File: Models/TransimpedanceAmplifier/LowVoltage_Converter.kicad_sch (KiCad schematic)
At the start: 6 parts, among them U7 LM78L05, 5V, 5%, U9 LM79L05, -5V, 5%

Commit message: Save progress after a major refactoring
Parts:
- removed C5: 10 nF, symbol Device:C
- removed C6: 100 nF, symbol Device:C
- removed D4, D5: D_Schottky, symbol Device:D_Schottky
- removed U7: LM78L05, 5V, 5%, LP3_TEX, symbol LM78L:LM78L05ACZ_LFT1
- removed U9: LM79L05, -5V, 5%, LP3_TEX, symbol LM79L:LM79L05ACZ_LFT1
- added C10: 10 nF, symbol Device:C
- added C9: 1 uF, symbol Device:C
- added D10, D11: D_Schottky, symbol Device:D_Schottky
- added U10: LM78L05, 5V, 5%, LP3_TEX, symbol LM78L:LM78L05ACZ_LFT1
- added U8: TLV76133, 3.3V, 1%, DCY0004A-IPC_A, symbol TLV761:PTLV76118DCYR
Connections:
- net 5V: now also C10.1, D10.1 (K), D11.1 (K), U10.1 (OUTPUT), U8.3 (IN)
- net GND: now also C10.2, C9.2, D11.2 (A), U10.2 (GND), U8.1 (GND)
- new net 18V: U10.3 (INPUT)
- new net 3.3V: C9.1, D10.2 (A), U8.4 (OUT)
- no-connect marks 0 -> 1
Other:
- note added: "Dropout voltage: 0.9 V (typical), 1.6 V (max) Variation with load: 0.9 V (1.0 A) 0.7 V (0.8 A) 0.2 V (0.1 A) Dropout voltage exceeds expected value when Vout + 1.5 V < 4.0 V"

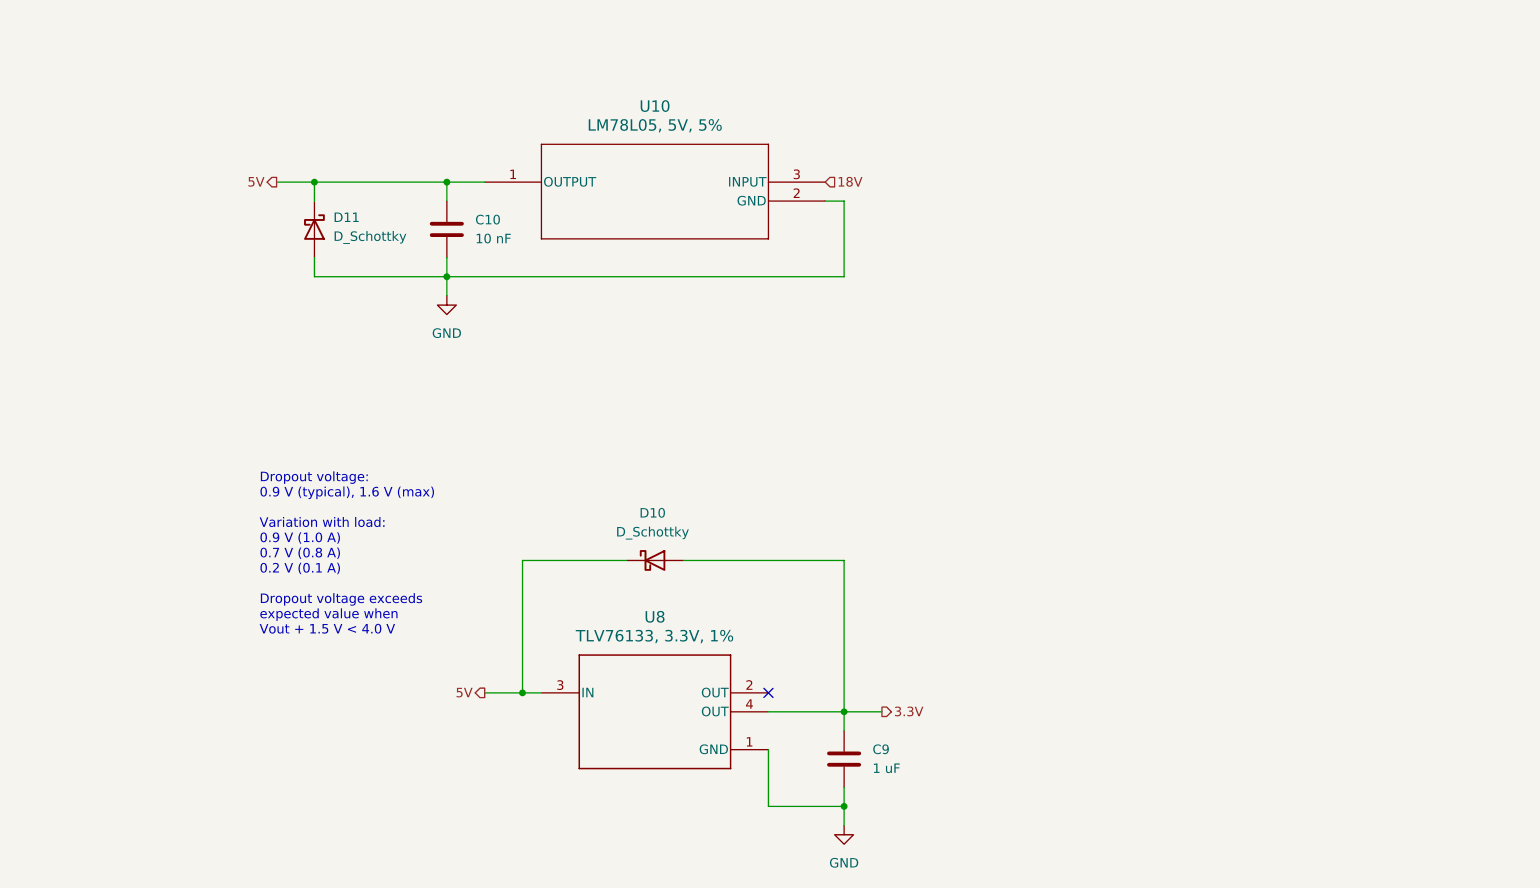
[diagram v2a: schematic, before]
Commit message: Added purchase links for all current capacitors, with dimensional tolerances matching the footprint
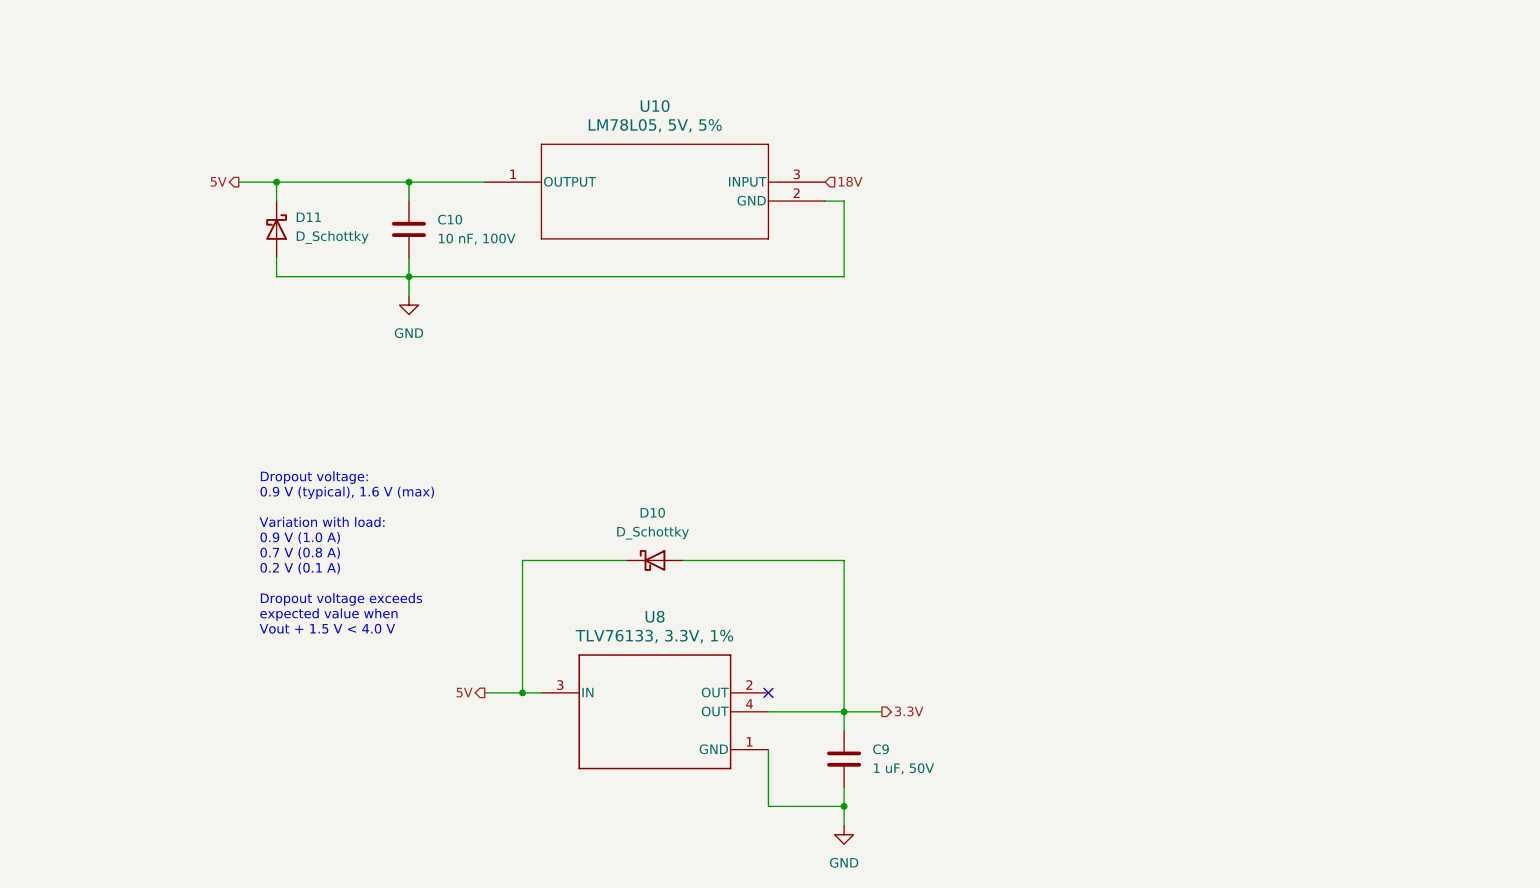
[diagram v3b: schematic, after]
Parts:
- C10: value 10 nF -> 10 nF, 100V; Purchase Link (none) -> https://www.digikey.com/en/products/detail/murata-electroni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
- C9: value 1 uF -> 1 uF, 50V; Purchase Link (none) -> https://www.digikey.com/en/products/detail/murata-electroni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
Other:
- moved on the sheet: C10, D11
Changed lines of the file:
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@@
 	)
 	(junction
-		(at 114.3 68.58)
+		(at 109.22 68.58)
 		(diameter 0)
 		(color 0 0 0 0)
 	)
 	(junction
-		(at 96.52 55.88)
+		(at 91.44 55.88)
 		(diameter 0)
 		(color 0 0 0 0)
 	)
 	(junction
-		(at 114.3 55.88)
+		(at 109.22 55.88)
 		(diameter 0)
 		(color 0 0 0 0)
@@
 	(wire
 		(pts
+			(xy 124.46 124.46) (xy 127 124.46)
+		)
+		(stroke
+			(width 0)
+			(type default)
+		)
+	)
+	(wire
+		(pts
+			(xy 167.64 127) (xy 167.64 129.54)
+		)
+		(stroke
+			(width 0)
+			(type default)
+		)
+	)
+	(wire
+		(pts
+			(xy 167.64 68.58) (xy 167.64 58.42)
+		)
+		(stroke
+			(width 0)
+			(type default)
+		)
+	)
+	(wire
+		(pts
+			(xy 119.38 124.46) (xy 124.46 124.46)
+		)
+		(stroke
+			(width 0)
+			(type default)
+		)
+	)
+	(wire
+		(pts
+			(xy 167.64 139.7) (xy 157.48 139.7)
+		)
+		(stroke
+			(width 0)
+			(type default)
+		)
+	)
+	(wire
+		(pts
+			(xy 138.43 106.68) (xy 124.46 106.68)
+		)
+		(stroke
+			(width 0)
+			(type default)
+		)
+	)
+	(wire
+		(pts
+			(xy 91.44 55.88) (xy 91.44 58.42)
+		)
+		(stroke
+			(width 0)
+			(type default)
+		)
+	)
+	(wire
+		(pts
+			(xy 157.48 127) (xy 167.64 127)
+		)
+		(stroke
+			(width 0)
+			(type default)
+		)
+	)
+	(wire
+		(pts
+			(xy 109.22 66.04) (xy 109.22 68.58)
+		)
+		(stroke
+			(width 0)
+			(type default)
+		)
+	)
+	(wire
+		(pts
+			(xy 109.22 55.88) (xy 119.38 55.88)
+		)
+		(stroke
+			(width 0)
+			(type default)
+		)
+	)
+	(wire
+		(pts
+			(xy 109.22 55.88) (xy 91.44 55.88)
+		)
+		(stroke
+			(width 0)
+			(type default)
+		)
+	)
+	(wire
+		(pts
+			(xy 167.64 137.16) (xy 167.64 139.7)
+		)
+		(stroke
+			(width 0)
+			(type default)
+		)
+	)
+	(wire
+		(pts
+			(xy 109.22 55.88) (xy 109.22 58.42)
+		)
+		(stroke
+			(width 0)
+			(type default)
+		)
+	)
+	(wire
+		(pts
 			(xy 165.1 58.42) (xy 167.64 58.42)
 		)
@@
 	(wire
 		(pts
-			(xy 124.46 124.46) (xy 127 124.46)
-		)
-		(stroke
-			(width 0)
-			(type default)
-		)
-	)
-	(wire
-		(pts
-			(xy 167.64 127) (xy 167.64 129.54)
-		)
-		(stroke
-			(width 0)
-			(type default)
-		)
-	)
-	(wire
-		(pts
-			(xy 119.38 124.46) (xy 124.46 124.46)
-		)
-		(stroke
-			(width 0)
-			(type default)
-		)
-	)
-	(wire
-		(pts
-			(xy 167.64 139.7) (xy 157.48 139.7)
-		)
-		(stroke
-			(width 0)
-			(type default)
-		)
-	)
-	(wire
-		(pts
-			(xy 138.43 106.68) (xy 124.46 106.68)
-		)
-		(stroke
-			(width 0)
-			(type default)
-		)
-	)
-	(wire
-		(pts
-			(xy 96.52 55.88) (xy 96.52 58.42)
-		)
-		(stroke
-			(width 0)
-			(type default)
-		)
-	)
-	(wire
-		(pts
-			(xy 114.3 68.58) (xy 167.64 68.58)
-		)
-		(stroke
-			(width 0)
-			(type default)
-		)
-	)
-	(wire
-		(pts
-			(xy 157.48 127) (xy 167.64 127)
-		)
-		(stroke
-			(width 0)
-			(type default)
-		)
-	)
-	(wire
-		(pts
-			(xy 114.3 66.04) (xy 114.3 68.58)
-		)
-		(stroke
-			(width 0)
-			(type default)
-		)
-	)
-	(wire
-		(pts
-			(xy 119.38 55.88) (xy 114.3 55.88)
-		)
-		(stroke
-			(width 0)
-			(type default)
-		)
-	)
-	(wire
-		(pts
-			(xy 114.3 55.88) (xy 96.52 55.88)
-		)
-		(stroke
-			(width 0)
-			(type default)
-		)
-	)
-	(wire
-		(pts
-			(xy 167.64 137.16) (xy 167.64 139.7)
-		)
-		(stroke
-			(width 0)
-			(type default)
-		)
-	)
-	(wire
-		(pts
-			(xy 114.3 55.88) (xy 114.3 58.42)
-		)
-		(stroke
-			(width 0)
-			(type default)
-		)
-	)
-	(wire
-		(pts
-			(xy 96.52 66.04) (xy 96.52 68.58)
+			(xy 109.22 68.58) (xy 167.64 68.58)
+		)
+		(stroke
+			(width 0)
+			(type default)
+		)
+	)
+	(wire
+		(pts
+			(xy 91.44 66.04) (xy 91.44 68.58)
 		)
 		(stroke
@@
 	(wire
 		(pts
-			(xy 91.44 55.88) (xy 96.52 55.88)
-		)
-		(stroke
-			(width 0)
-			(type default)
-		)
-	)
-	(wire
-		(pts
-			(xy 167.64 68.58) (xy 167.64 58.42)
+			(xy 86.36 55.88) (xy 91.44 55.88)
 		)
 		(stroke
@@
 	(wire
 		(pts
-			(xy 114.3 68.58) (xy 114.3 71.12)
-		)
-		(stroke
-			(width 0)
-			(type default)
-		)
-	)
-	(wire
-		(pts
-			(xy 96.52 68.58) (xy 114.3 68.58)
+			(xy 109.22 68.58) (xy 109.22 71.12)
+		)
+		(stroke
+			(width 0)
+			(type default)
+		)
+	)
+	(wire
+		(pts
+			(xy 91.44 68.58) (xy 109.22 68.58)
 		)
 		(stroke
@@
 	(hierarchical_label "5V"
 		(shape output)
-		(at 91.44 55.88 180)
+		(at 86.36 55.88 180)
 		(effects
 			(font
@@
 	(symbol
 		(lib_id "Device:C")
-		(at 114.3 62.23 0)
+		(at 109.22 62.23 0)
 		(unit 1)
 		(exclude_from_sim no)
@@
 		(fields_autoplaced yes)
 		(property "Reference" "C10"
-			(at 118.11 60.9599 0)
+			(at 113.03 60.9599 0)
 			(effects
 				(font
@@
 			)
 		)
-		(property "Value" "10 nF"
-			(at 118.11 63.4999 0)
+		(property "Value" "10 nF, 100V"
+			(at 113.03 63.4999 0)
 			(effects
 				(font
@@
 		)
 		(property "Footprint" ""
-			(at 115.2652 66.04 0)
+			(at 110.1852 66.04 0)
 			(effects
 				(font
@@
 		)
 		(property "Datasheet" "~"
-			(at 114.3 62.23 0)
+			(at 109.22 62.23 0)
 			(effects
 				(font
@@
 		)
 		(property "Description" "Unpolarized capacitor"
-			(at 114.3 62.23 0)
+			(at 109.22 62.23 0)
+			(effects
+				(font
+					(size 1.27 1.27)
+				)
+				(hide yes)
+			)
+		)
+		(property "Purchase Link" "https://www.digikey.com/en/products/detail/murata-electronics/GCM188R72A103KA37D/1641655"
+			(at 109.22 62.23 0)
 			(effects
 				(font
@@
 	(symbol
 		(lib_id "power:GND")
-		(at 114.3 71.12 0)
+		(at 109.22 71.12 0)
 		(unit 1)
 		(exclude_from_sim no)
@@
 		(fields_autoplaced yes)
 		(property "Reference" "#PWR015"
-			(at 114.3 77.47 0)
+			(at 109.22 77.47 0)
 			(effects
 				(font
@@
 		)
 		(property "Value" "GND"
-			(at 114.3 76.2 0)
+			(at 109.22 76.2 0)
 			(effects
 				(font
@@
 		)
 		(property "Footprint" ""
-			(at 114.3 71.12 0)
+			(at 109.22 71.12 0)
 			(effects
 				(font
@@
 		)
 		(property "Datasheet" ""
-			(at 114.3 71.12 0)
+			(at 109.22 71.12 0)
 			(effects
 				(font
@@
 		)
 		(property "Description" "Power symbol creates a global label with name \"GND\" , ground"
-			(at 114.3 71.12 0)
+			(at 109.22 71.12 0)
 			(effects
 				(font
@@
 	(symbol
 		(lib_id "Device:D_Schottky")
-		(at 96.52 62.23 270)
+		(at 91.44 62.23 270)
 		(unit 1)
 		(exclude_from_sim no)
@@
 		(fields_autoplaced yes)
 		(property "Reference" "D11"
-			(at 99.06 60.6424 90)
+			(at 93.98 60.6424 90)
 			(effects
 				(font
@@
 		)
 		(property "Value" "D_Schottky"
-			(at 99.06 63.1824 90)
+			(at 93.98 63.1824 90)
 			(effects
 				(font
@@
 		)
 		(property "Footprint" ""
-			(at 96.52 62.23 0)
+			(at 91.44 62.23 0)
 			(effects
 				(font
@@
 		)
 		(property "Datasheet" "~"
-			(at 96.52 62.23 0)
+			(at 91.44 62.23 0)
 			(effects
 				(font
@@
 		)
 		(property "Description" "Schottky diode"
-			(at 96.52 62.23 0)
+			(at 91.44 62.23 0)
 			(effects
 				(font
@@
 			)
 		)
-		(property "Value" "1 uF"
+		(property "Value" "1 uF, 50V"
 			(at 171.45 134.6199 0)
 			(effects
@@
 			(at 167.64 133.35 0)
 			(effects
+				(font
+					(size 1.27 1.27)
+				)
+				(hide yes)
+			)
+		)
+		(property "Purchase Link" "https://www.digikey.com/en/products/detail/murata-electronics/GRT188R61H105KE13D/5416752"
+			(at 167.64 133.35 0)
+			(effects

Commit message: All suppliers are out of stock of LM7915L in the simple TO-92-3 package. Resolve this by first tabulating the maximum possible current on each regulator.
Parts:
- U10: Purchase Link (none) -> https://www.digikey.com/en/products/detail/texas-instrument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
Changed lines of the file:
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@@
 			)
 		)
-		(property "Purchase Link" ""
+		(property "Purchase Link" "https://www.digikey.com/en/products/detail/texas-instruments/LM78L05ACZ-NOPB/6333"
 			(at 119.38 55.88 0)
 			(effects

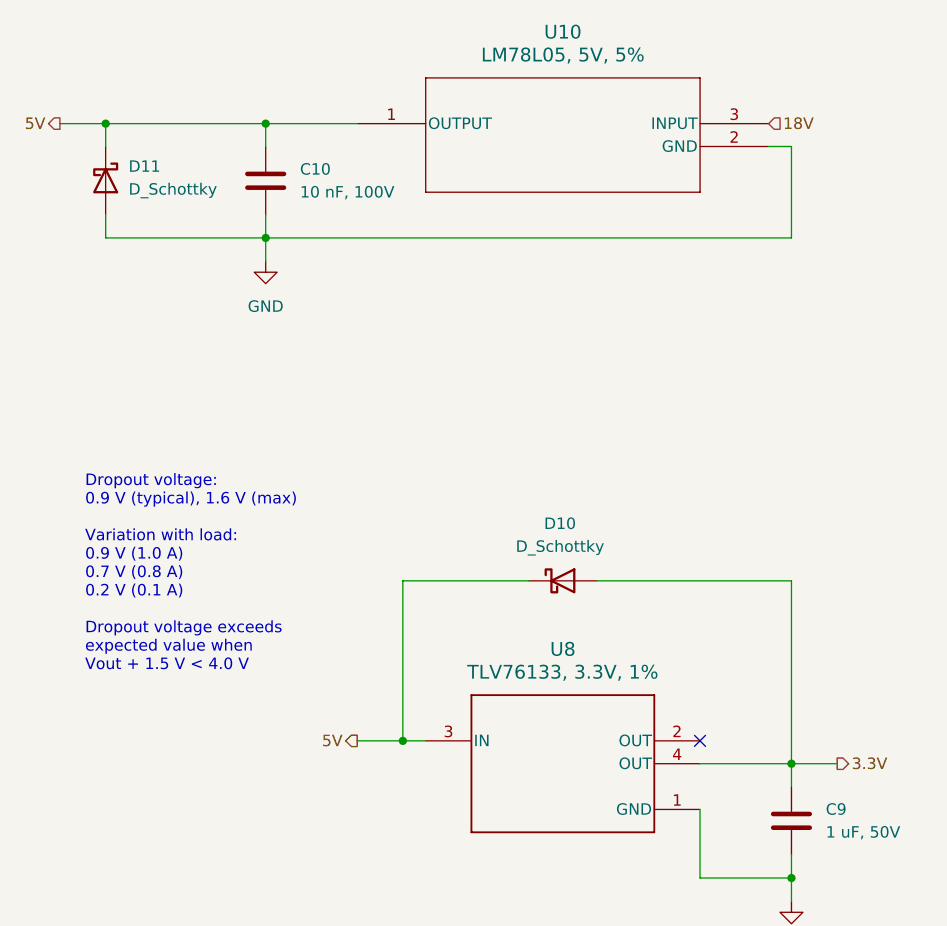
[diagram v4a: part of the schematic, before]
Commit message: Removed all protection diodes for now
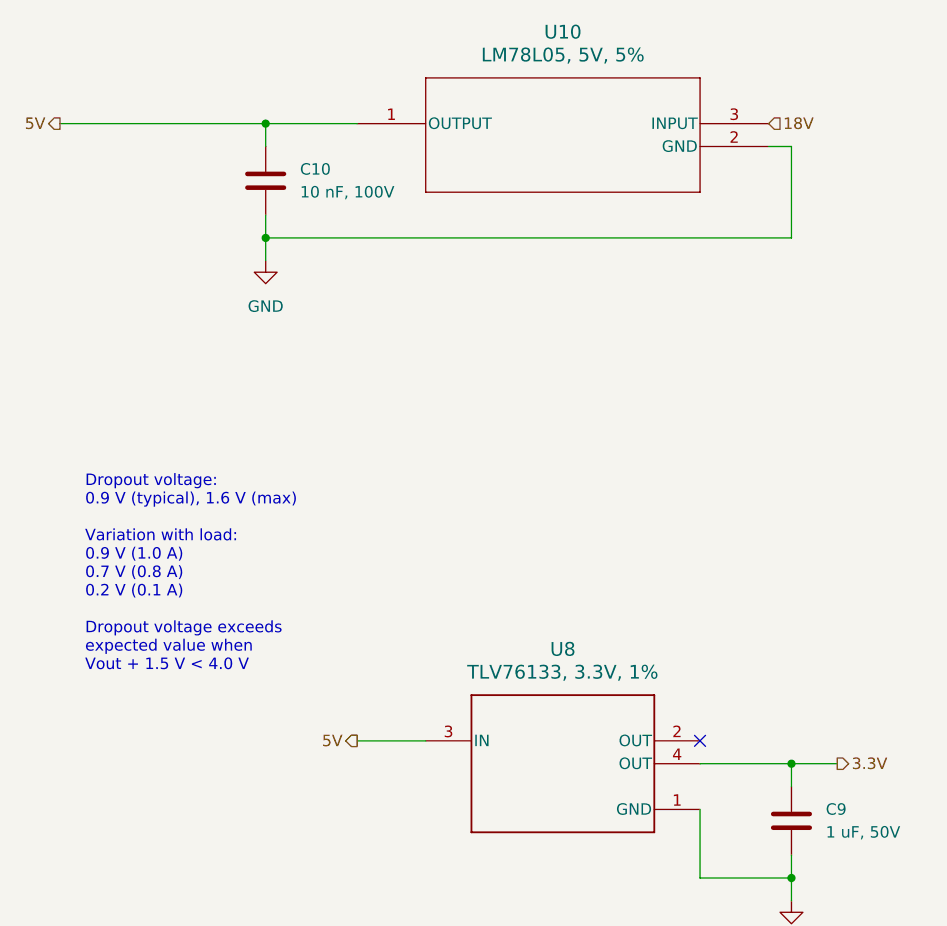
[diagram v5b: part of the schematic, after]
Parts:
- removed D10, D11: D_Schottky, symbol Device:D_Schottky
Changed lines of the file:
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@@
-	)
-	(junction
-		(at 124.46 124.46)
-		(diameter 0)
-		(color 0 0 0 0)
 	)
 	(junction
@@
 	)
 	(junction
-		(at 91.44 55.88)
-		(diameter 0)
-		(color 0 0 0 0)
-	)
-	(junction
 		(at 109.22 55.88)
 		(diameter 0)
@@
 	(wire
 		(pts
-			(xy 124.46 106.68) (xy 124.46 124.46)
-		)
-		(stroke
-			(width 0)
-			(type default)
-		)
-	)
-	(wire
-		(pts
-			(xy 124.46 124.46) (xy 127 124.46)
+			(xy 119.38 124.46) (xy 127 124.46)
 		)
 		(stroke
@@
 	(wire
 		(pts
-			(xy 119.38 124.46) (xy 124.46 124.46)
-		)
-		(stroke
-			(width 0)
-			(type default)
-		)
-	)
-	(wire
-		(pts
 			(xy 167.64 139.7) (xy 157.48 139.7)
 		)
@@
 	(wire
 		(pts
-			(xy 138.43 106.68) (xy 124.46 106.68)
-		)
-		(stroke
-			(width 0)
-			(type default)
-		)
-	)
-	(wire
-		(pts
-			(xy 91.44 55.88) (xy 91.44 58.42)
-		)
-		(stroke
-			(width 0)
-			(type default)
-		)
-	)
-	(wire
-		(pts
 			(xy 157.48 127) (xy 167.64 127)
 		)
@@
 	(wire
 		(pts
-			(xy 109.22 55.88) (xy 91.44 55.88)
+			(xy 86.36 55.88) (xy 109.22 55.88)
 		)
 		(stroke
@@
 	(wire
 		(pts
-			(xy 91.44 66.04) (xy 91.44 68.58)
-		)
-		(stroke
-			(width 0)
-			(type default)
-		)
-	)
-	(wire
-		(pts
-			(xy 146.05 106.68) (xy 167.64 106.68)
-		)
-		(stroke
-			(width 0)
-			(type default)
-		)
-	)
-	(wire
-		(pts
-			(xy 86.36 55.88) (xy 91.44 55.88)
-		)
-		(stroke
-			(width 0)
-			(type default)
-		)
-	)
-	(wire
-		(pts
 			(xy 157.48 132.08) (xy 157.48 139.7)
 		)
@@
 	(wire
 		(pts
-			(xy 167.64 127) (xy 167.64 106.68)
-		)
-		(stroke
-			(width 0)
-			(type default)
-		)
-	)
-	(wire
-		(pts
 			(xy 167.64 127) (xy 172.72 127)
 		)
@@
 		(pts
 			(xy 109.22 68.58) (xy 109.22 71.12)
-		)
-		(stroke
-			(width 0)
-			(type default)
-		)
-	)
-	(wire
-		(pts
-			(xy 91.44 68.58) (xy 109.22 68.58)
 		)
 		(stroke
@@
 	)
 	(symbol
-		(lib_id "Device:D_Schottky")
-		(at 142.24 106.68 0)
-		(unit 1)
-		(exclude_from_sim no)
-		(in_bom yes)
-		(on_board yes)
-		(dnp no)
-		(fields_autoplaced yes)
-		(property "Reference" "D10"
-			(at 141.9225 100.33 0)
-			(effects
-				(font
-					(size 1.27 1.27)
-				)
-			)
-		)
-		(property "Value" "D_Schottky"
-			(at 141.9225 102.87 0)
-			(effects
-				(font
-					(size 1.27 1.27)
-				)
-			)
-		)
-		(property "Footprint" ""
-			(at 142.24 106.68 0)
-			(effects
-				(font
-					(size 1.27 1.27)
-				)
-				(hide yes)
-			)
-		)
-		(property "Datasheet" "~"
-			(at 142.24 106.68 0)
-			(effects
-				(font
-					(size 1.27 1.27)
-				)
-				(hide yes)
-			)
-		)
-		(property "Description" "Schottky diode"
-			(at 142.24 106.68 0)
-			(effects
-				(font
-					(size 1.27 1.27)
-				)
-				(hide yes)
-			)
-		)
-		(pin "2"
-		)
-		(pin "1"
-		)
-		(instances
-			(project ""
-				(path "/ec9f2ae3-e40d-40eb-9760-2b611ee8efd1/d0ece2d4-5b22-4822-ad0c-e2361683ec3d/8db21157-4c7b-40b0-8814-5c9be8b7a36f"
-					(reference "D10")
-					(unit 1)
-				)
-			)
-		)
-	)
-	(symbol
 		(lib_id "power:GND")
 		(at 109.22 71.12 0)
@@
 					(unit 1)
 				)
-			)
-		)
-	)
-	(symbol
-		(lib_id "Device:D_Schottky")
-		(at 91.44 62.23 270)
-		(unit 1)
-		(exclude_from_sim no)
-		(in_bom yes)
-		(on_board yes)
-		(dnp no)
-		(fields_autoplaced yes)
-		(property "Reference" "D11"
-			(at 93.98 60.6424 90)
-			(effects
-				(font
-					(size 1.27 1.27)
-				)
-				(justify left)
-			)
-		)
-		(property "Value" "D_Schottky"
-			(at 93.98 63.1824 90)
-			(effects
-				(font
-					(size 1.27 1.27)
-				)
-				(justify left)
-			)
-		)
-		(property "Footprint" ""
-			(at 91.44 62.23 0)
-			(effects
-				(font
-					(size 1.27 1.27)
-				)
-				(hide yes)
-			)
-		)
-		(property "Datasheet" "~"
-			(at 91.44 62.23 0)
-			(effects
-				(font
-					(size 1.27 1.27)
-				)
-				(hide yes)
-			)
-		)
-		(property "Description" "Schottky diode"
-			(at 91.44 62.23 0)
-			(effects
-				(font
-					(size 1.27 1.27)
-				)
-				(hide yes)
-			)
-		)
-		(pin "1"
-		)
-		(pin "2"
-		)
-		(instances
-			(project "TransimpedanceAmplifier"
-				(path "/ec9f2ae3-e40d-40eb-9760-2b611ee8efd1/d0ece2d4-5b22-4822-ad0c-e2361683ec3d/8db21157-4c7b-40b0-8814-5c9be8b7a36f"
-					(reference "D11")
-					(unit 1)
-				)
